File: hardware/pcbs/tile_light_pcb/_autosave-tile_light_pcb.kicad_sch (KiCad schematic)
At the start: 33 parts, among them CN1 ZX-ZH1.5-5PLT, CN2 ZX-ZH1.5-5PLT, CN3 ZX-ZH1.5-2PLT, CN4 ZX-ZH1.5-2PLT, CN5 ZX-ZH1.5-2PLT, SW1 HX-6X6X7.3-TP FT SQUARE BUTTON, SW2 HX-6X6X7.3-TP FT SQUARE BUTTON

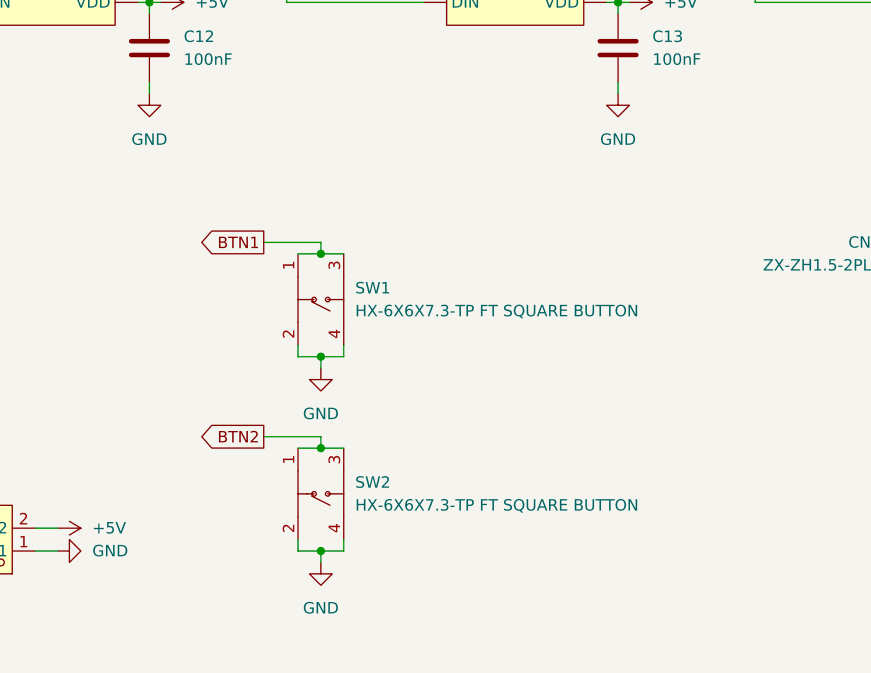
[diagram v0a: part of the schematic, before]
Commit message: hardware: tile light pcb: Finished revA of pcb
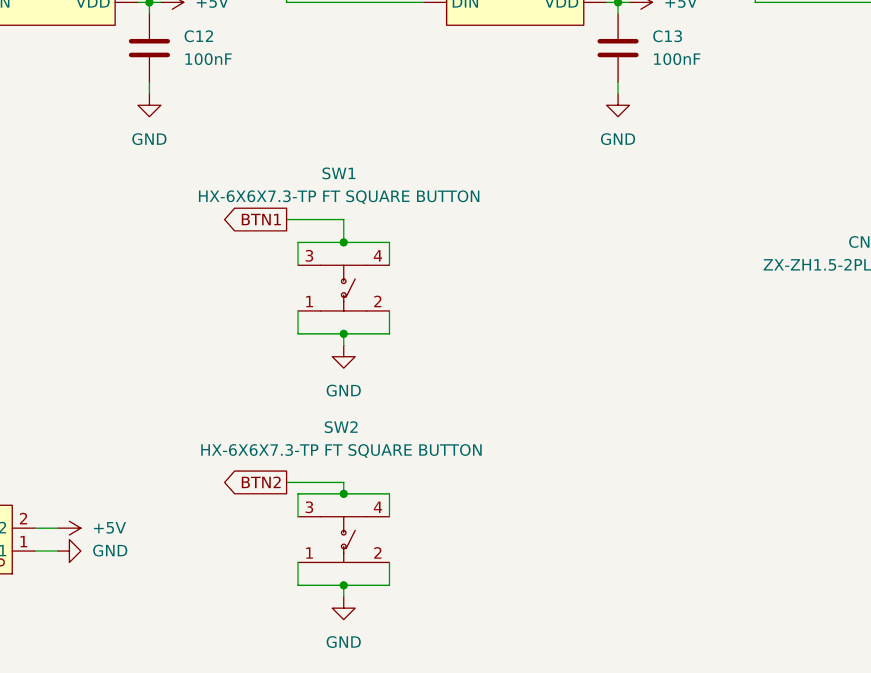
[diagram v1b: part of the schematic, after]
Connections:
- net BTN1: now also SW1.4; no longer SW1.1
- net BTN2: now also SW2.4; no longer SW2.1
- net GND: now also SW1.1, SW2.1; no longer SW1.4, SW2.4
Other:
- moved on the sheet: SW1, SW2
